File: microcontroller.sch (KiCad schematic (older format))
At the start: 18 parts, among them J6 I2C, J7 Conn_01x02, SW1 SW_Push, U3 ESP32-DEVKIT

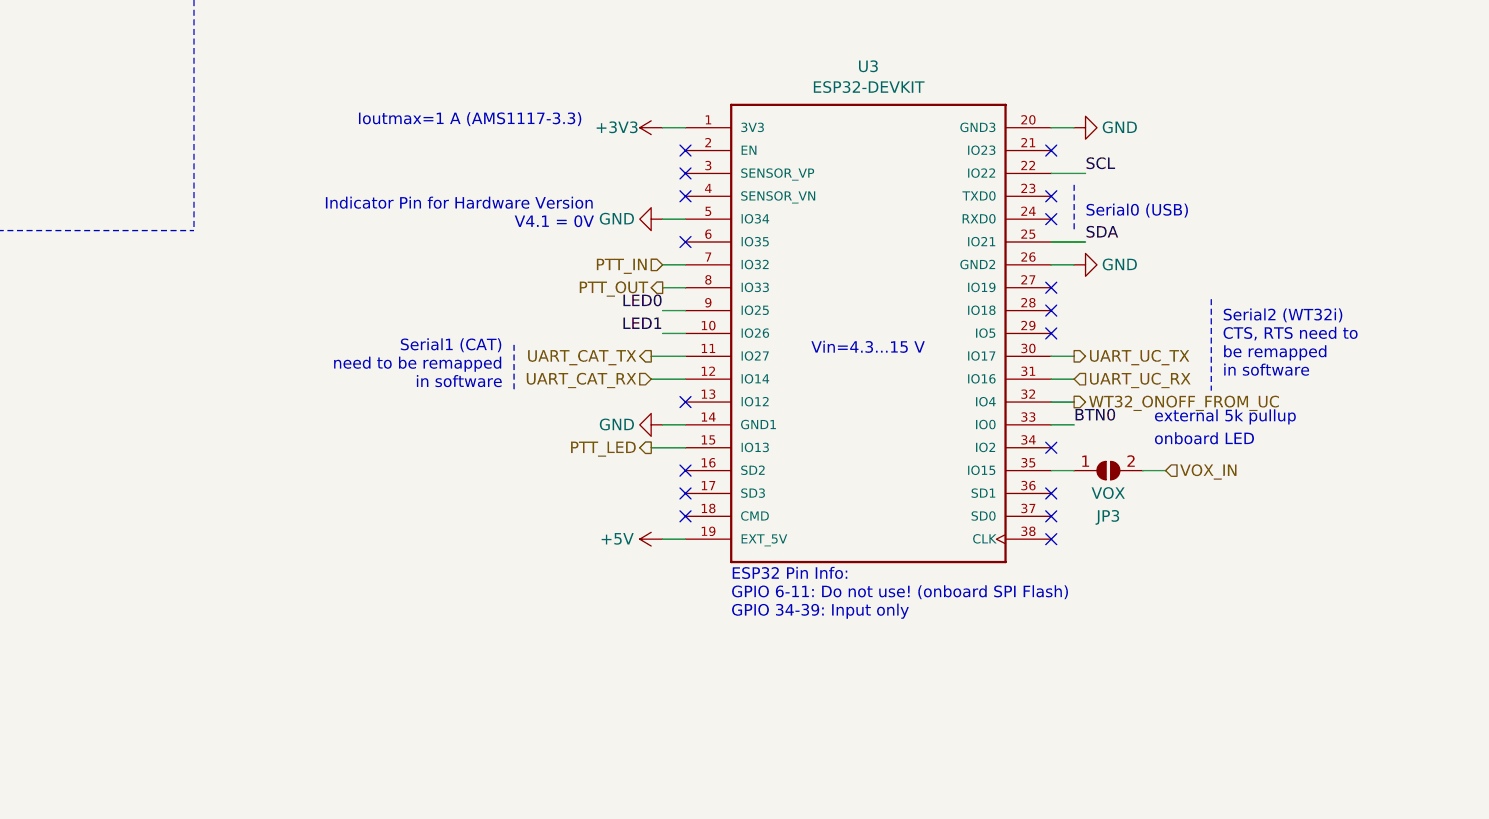
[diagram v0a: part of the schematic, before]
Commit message: Adding annotations for ADC1/2
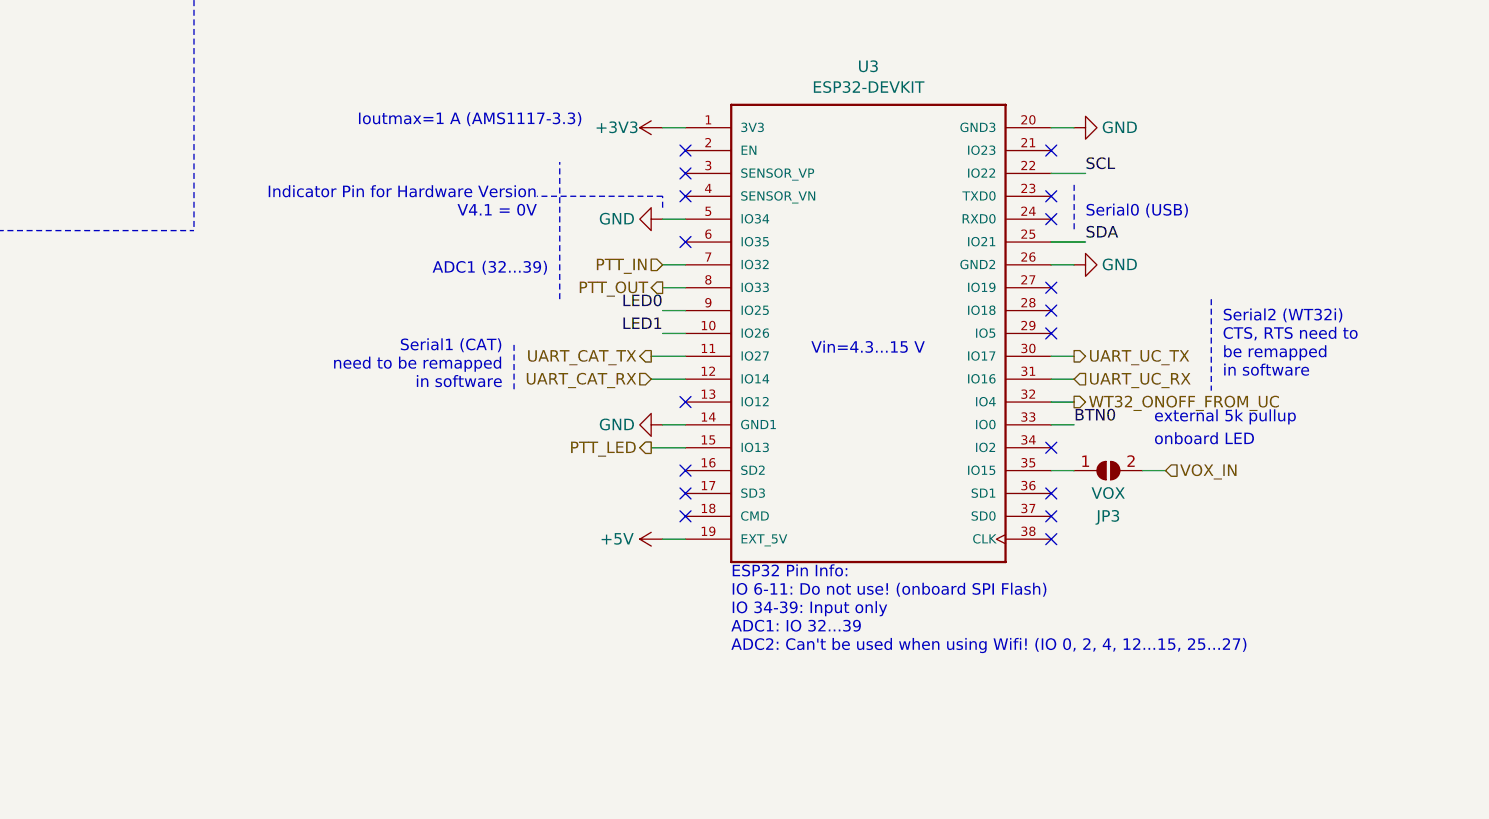
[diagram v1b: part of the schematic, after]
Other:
- note added: "ADC1 (32...39)"
- note added: "ESP32 Pin Info:\nIO 6-11: Do not use! (onboard SPI Flash)\nIO 34-39: Input only\nADC1: IO 32...39\nADC2: Can't be used when using Wifi! (IO 0, 2, 4, 12...15, 25...27)"
- note removed: "ESP32 Pin Info:\nGPIO 6-11: Do not use! (onboard SPI Flash)\nGPIO 34-39: Input only\n"
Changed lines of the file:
@@
 EESchema Schematic File Version 4
 LIBS:bt-trx-dev-board-cache
-EELAYER 30 0
+EELAYER 29 0
 EELAYER END
 $Descr A4 11693 8268
@@
 NoConn ~ 6900 1500
 NoConn ~ 6900 1600
-Text Notes 7100 3450 0    50   ~ 0
-ESP32 Pin Info:\nGPIO 6-11: Do not use! (onboard SPI Flash)\nGPIO 34-39: Input only\n
+Text Notes 7100 3600 0    50   ~ 0
+ESP32 Pin Info:\nIO 6-11: Do not use! (onboard SPI Flash)\nIO 34-39: Input only\nADC1: IO 32...39\nADC2: Can't be used when using Wifi! (IO 0, 2, 4, 12...15, 25...27)
 Wire Wire Line
 	8500 1300 8600 1300
@@
 	0    -1   -1   0
 $EndComp
-Text Notes 6500 1750 2    50   ~ 0
+Text Notes 6250 1700 2    50   ~ 0
 Indicator Pin for Hardware Version\nV4.1 = 0V
 Text HLabel 6750 2700 0    50   Output ~ 0
@@
 Wire Wire Line
 	8900 2800 9000 2800
+Wire Notes Line
+	6350 2050 6350 1450
+Text Notes 6300 1950 2    50   ~ 0
+ADC1 (32...39)
+Wire Notes Line style solid
+	6800 1650 6800 1600
+Wire Notes Line style solid
+	6800 1600 6250 1600
 $EndSCHEMATC

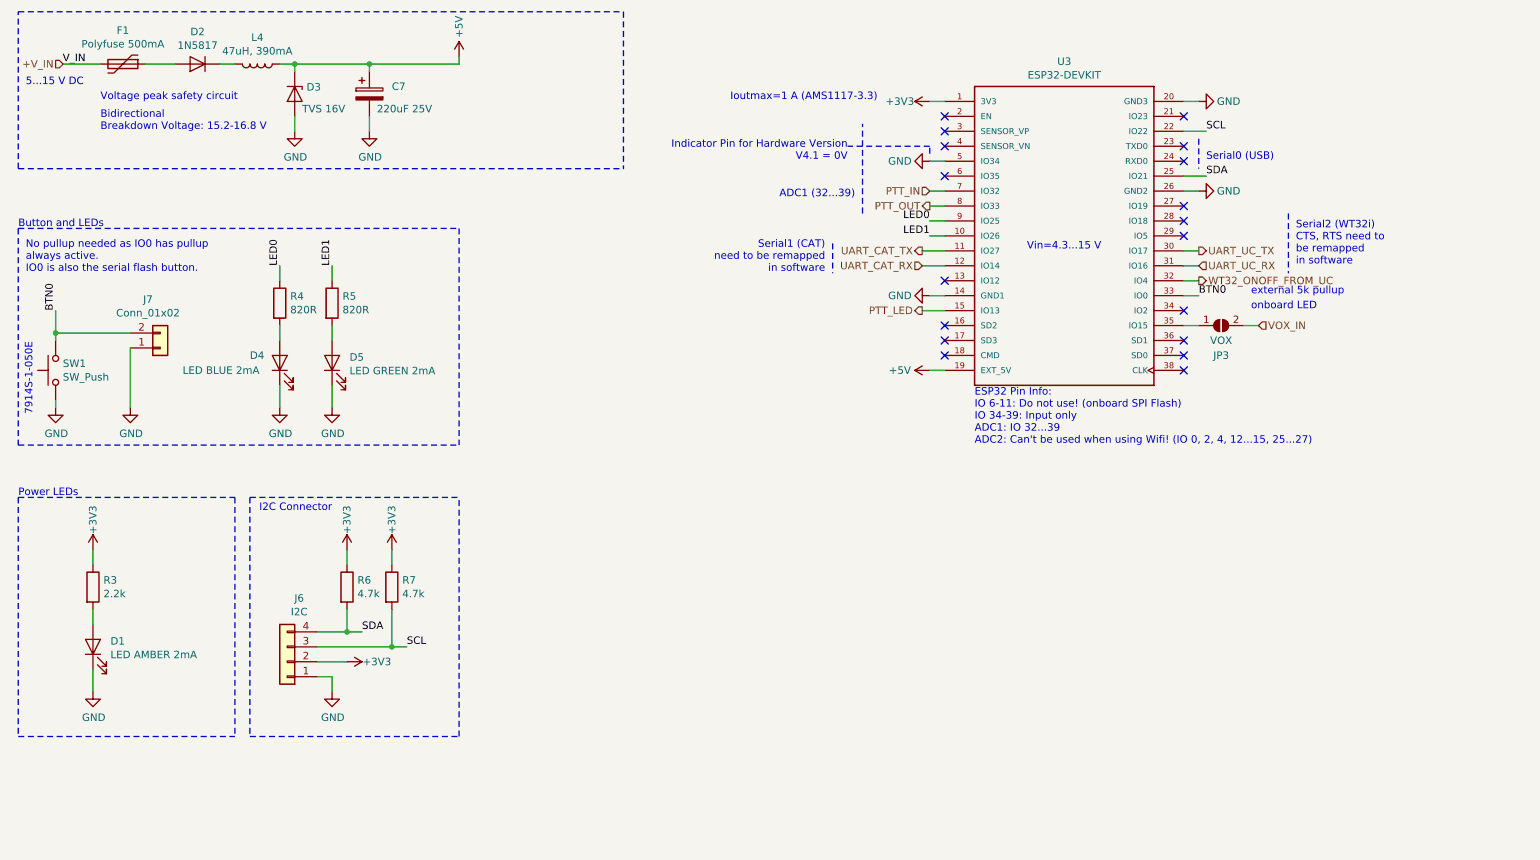
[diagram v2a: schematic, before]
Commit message: [#16] Move SW1 and VOX to usable Pins
* Moved SW1 form GPIO0 to GPIO18
* Added Pullup to SW1
* Moved VOX form GPIO2 to GPIO35
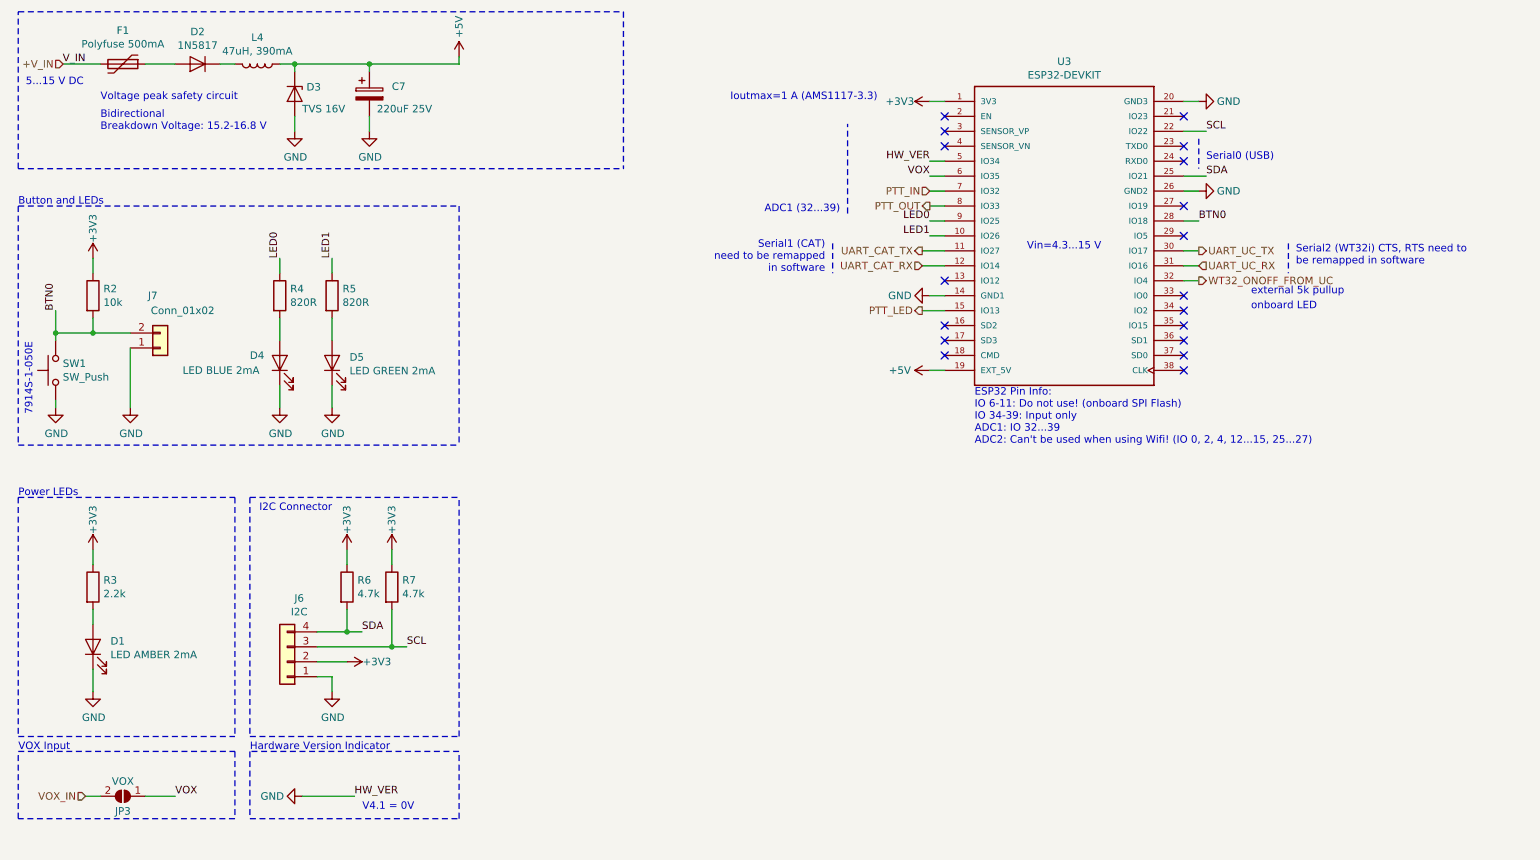
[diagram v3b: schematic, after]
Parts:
- added R2: 10k, Resistor_SMD:R_0805_2012Metric_Pad1.15x1.40mm_HandSolder, symbol Device:R
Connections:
- net +3V3: now also R2.1
- net BTN0: now also U3.28 (IO18), R2.2; no longer U3.33 (IO0)
- net at U3.35 (IO15): no longer JP3.1 (A)
- net VOX: now reaches U3.6 (IO35)
- net VOX: now also JP3.1 (A)
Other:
- note added: "Hardware Version Indicator"
- note added: "Serial2 (WT32i) CTS, RTS need to\nbe remapped in software"
- note added: "V4.1 = 0V"
- note added: "VOX Input"
- note removed: "Indicator Pin for Hardware Version\nV4.1 = 0V"
- note removed: "No pullup needed as IO0 has pullup\nalways active.\nIO0 is also the serial flash button."
- note removed: "Serial2 (WT32i)\nCTS, RTS need to\nbe remapped \nin software"
- moved on the sheet: JP3, R4, R5
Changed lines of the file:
@@
 L Device:R R?
 U 1 1 5C1540D9
-P 2450 2650
+P 2450 2600
 AR Path="/5C1540D9" Ref="R?"  Part="1"
 AR Path="/5C10B93A/5C1540D9" Ref="R4"  Part="1"
-F 0 "R4" H 2520 2696 50  0000 L CNN
-F 1 "820R" H 2520 2605 50  0000 L CNN
-F 2 "Resistor_SMD:R_0805_2012Metric_Pad1.15x1.40mm_HandSolder" V 2380 2650 50  0001 C CNN
-F 3 "~" H 2450 2650 50  0001 C CNN
-F 4 "603-RC0805JR-07820RL" H -2300 -2500 50  0001 C CNN "Mouser Best.Nr."
-	1    2450 2650
+F 0 "R4" H 2520 2646 50  0000 L CNN
+F 1 "820R" H 2520 2555 50  0000 L CNN
+F 2 "Resistor_SMD:R_0805_2012Metric_Pad1.15x1.40mm_HandSolder" V 2380 2600 50  0001 C CNN
+F 3 "~" H 2450 2600 50  0001 C CNN
+F 4 "603-RC0805JR-07820RL" H -2300 -2550 50  0001 C CNN "Mouser Best.Nr."
+	1    2450 2600
 	1    0    0    -1
 $EndComp
@@
 	2450 3200 2450 3350
 Wire Wire Line
-	2450 2500 2450 2400
-Text Label 2450 2400 1    50   ~ 0
+	2450 2450 2450 2350
+Text Label 2450 2350 1    50   ~ 0
 LED0
 $Comp
 L Device:R R?
 U 1 1 5C1540F1
-P 2800 2650
+P 2800 2600
 AR Path="/5C1540F1" Ref="R?"  Part="1"
 AR Path="/5C10B93A/5C1540F1" Ref="R5"  Part="1"
-F 0 "R5" H 2870 2696 50  0000 L CNN
-F 1 "820R" H 2870 2605 50  0000 L CNN
-F 2 "Resistor_SMD:R_0805_2012Metric_Pad1.15x1.40mm_HandSolder" V 2730 2650 50  0001 C CNN
-F 3 "~" H 2800 2650 50  0001 C CNN
-F 4 "603-RC0805JR-07820RL" H -2300 -2500 50  0001 C CNN "Mouser Best.Nr."
-	1    2800 2650
+F 0 "R5" H 2870 2646 50  0000 L CNN
+F 1 "820R" H 2870 2555 50  0000 L CNN
+F 2 "Resistor_SMD:R_0805_2012Metric_Pad1.15x1.40mm_HandSolder" V 2730 2600 50  0001 C CNN
+F 3 "~" H 2800 2600 50  0001 C CNN
+F 4 "603-RC0805JR-07820RL" H -2300 -2550 50  0001 C CNN "Mouser Best.Nr."
+	1    2800 2600
 	1    0    0    -1
 $EndComp
@@
 	2800 3200 2800 3350
 Wire Wire Line
-	2800 2800 2800 2900
-Wire Wire Line
-	2800 2500 2800 2400
-Text Label 2800 2400 1    50   ~ 0
+	2800 2450 2800 2350
+Text Label 2800 2350 1    50   ~ 0
 LED1
-Wire Notes Line
-	3650 2150 3650 3600
-Wire Notes Line
-	700  2150 700  3600
-Text Notes 700  2150 0    50   ~ 0
+Text Notes 700  2000 0    50   ~ 0
 Button and LEDs
 Text HLabel 1000 1050 0    50   Input ~ 0
@@
 Text HLabel 8600 2500 2    50   Output ~ 0
 WT32_ONOFF_FROM_UC
-Text Label 8600 2600 0    50   ~ 0
-BTN0
 Wire Wire Line
 	6800 2200 6900 2200
@@
 7914S-1-050E
 Wire Wire Line
-	2450 2800 2450 2900
-Wire Wire Line
 	1200 4700 1200 4800
 Text Notes 9250 2400 0    50   ~ 0
-Serial2 (WT32i)\nCTS, RTS need to\nbe remapped \nin software
+Serial2 (WT32i) CTS, RTS need to\nbe remapped in software
 Wire Notes Line
 	6150 2250 6150 2450
@@
 Text Notes 8950 2600 0    50   ~ 0
 external 5k pullup
-Wire Notes Line
-	9200 2050 9200 2450
 Wire Wire Line
 	8500 2300 8600 2300
@@
 NoConn ~ 8500 2000
 NoConn ~ 6900 2500
-NoConn ~ 8500 2100
+NoConn ~ 8500 2800
 Wire Wire Line
 	8500 2500 8600 2500
@@
 NoConn ~ 8500 2200
 Wire Wire Line
-	8500 2600 8600 2600
-Text Notes 750  2450 0    50   ~ 0
-No pullup needed as IO0 has pullup\nalways active.\nIO0 is also the serial flash button.
+	8500 2100 8600 2100
 $Comp
 L ESP32-DEVKITC-32D:ESP32-DEVKITC-32D U3
@@
 $EndComp
 Wire Notes Line
-	700  2150 3650 2150
+	700  2000 3650 2000
 Wire Notes Line
 	700  3600 3650 3600
@@
 U 1 1 5D923484
 P 1650 2950
-F 0 "J7" H 1568 2625 50  0000 C CNN
-F 1 "Conn_01x02" H 1568 2716 50  0000 C CNN
+F 0 "J7" H 1600 2600 50  0000 C CNN
+F 1 "Conn_01x02" H 1800 2700 50  0000 C CNN
 F 2 "Connector_PinHeader_2.54mm:PinHeader_1x02_P2.54mm_Vertical" H 1650 2950 50  0001 C CNN
 F 3 "~" H 1650 2950 50  0001 C CNN
@@
 	950  2700 950  2850
 Wire Wire Line
-	1450 2850 950  2850
+	1450 2850 1200 2850
 Connection ~ 950  2850
 Wire Wire Line
@@
 Wire Wire Line
 	1550 1050 1750 1050
-Wire Wire Line
-	6900 1700 6800 1700
 $Comp
 L power:GND #PWR?
 U 1 1 5D8F131B
-P 6800 1700
+P 2600 5950
 AR Path="/5D8F131B" Ref="#PWR?"  Part="1"
 AR Path="/5C10B93A/5D8F131B" Ref="#PWR0101"  Part="1"
-F 0 "#PWR0101" H 6800 1450 50  0001 C CNN
-F 1 "GND" V 6800 1500 50  0000 C CNN
-F 2 "" H 6800 1700 50  0001 C CNN
-F 3 "" H 6800 1700 50  0001 C CNN
-	1    6800 1700
+F 0 "#PWR0101" H 2600 5700 50  0001 C CNN
+F 1 "GND" V 2600 5750 50  0000 C CNN
+F 2 "" H 2600 5950 50  0001 C CNN
+F 3 "" H 2600 5950 50  0001 C CNN
+	1    2600 5950
 	0    1    1    0
 $EndComp
@@
 	0    -1   -1   0
 $EndComp
-Text Notes 6250 1700 2    50   ~ 0
-Indicator Pin for Hardware Version\nV4.1 = 0V
+Text Notes 3350 6050 2    50   ~ 0
+V4.1 = 0V
 Text HLabel 6750 2700 0    50   Output ~ 0
 PTT_LED
-NoConn ~ 6900 1800
 Wire Wire Line
 	6750 2700 6900 2700
-Text HLabel 9000 2800 2    50   Input ~ 0
+Text HLabel 1150 5950 0    50   Input ~ 0
 VOX_IN
 $Comp
 L Jumper:SolderJumper_2_Open JP3
 U 1 1 5D943D8B
-P 8750 2800
-F 0 "JP3" H 8750 2600 50  0000 C CNN
-F 1 "VOX" H 8750 2700 50  0000 C CNN
-F 2 "Jumper:SolderJumper-2_P1.3mm_Open_TrianglePad1.0x1.5mm" H 8750 2800 50  0001 C CNN
-F 3 "~" H 8750 2800 50  0001 C CNN
-	1    8750 2800
-	1    0    0    -1
+P 1400 5950
+F 0 "JP3" H 1400 6050 50  0000 C CNN
+F 1 "VOX" H 1400 5850 50  0000 C CNN
+F 2 "Jumper:SolderJumper-2_P1.3mm_Open_TrianglePad1.0x1.5mm" H 1400 5950 50  0001 C CNN
+F 3 "~" H 1400 5950 50  0001 C CNN
+	1    1400 5950
+	-1   0    0    1
 $EndComp
 NoConn ~ 8500 2700
 Wire Wire Line
-	8500 2800 8600 2800
-Wire Wire Line
-	8900 2800 9000 2800
-Wire Notes Line
-	6350 2050 6350 1450
-Text Notes 6300 1950 2    50   ~ 0
+	6900 1800 6800 1800
+Wire Wire Line
+	1250 5950 1150 5950
+Wire Notes Line
+	6250 2050 6250 1450
+Text Notes 6200 2050 2    50   ~ 0
 ADC1 (32...39)
-Wire Notes Line style solid
-	6800 1650 6800 1600
-Wire Notes Line style solid
-	6800 1600 6250 1600
+Wire Notes Line
+	9200 2250 9200 2450
+Text Label 8600 2100 0    50   ~ 0
+BTN0
+NoConn ~ 8500 2600
+Text Label 6800 1800 2    50   ~ 0
+VOX
+Wire Wire Line
+	2600 5950 2950 5950
+Wire Wire Line
+	1550 5950 1750 5950
+Text Label 1750 5950 0    50   ~ 0
+VOX
+Wire Notes Line
+	700  5650 2150 5650
+Wire Notes Line
+	2150 5650 2150 6100
+Wire Notes Line
+	2150 6100 700  6100
+Wire Notes Line
+	700  6100 700  5650
+Text Notes 700  5650 0    50   ~ 0
+VOX Input
+Wire Notes Line
+	2250 5650 2250 6100
+Wire Notes Line
+	2250 6100 3650 6100
+Wire Notes Line
+	3650 6100 3650 5650
+Wire Notes Line
+	3650 5650 2250 5650
+Text Notes 2250 5650 0    50   ~ 0
+Hardware Version Indicator
+Text Label 2950 5950 0    50   ~ 0
+HW_VER
+Wire Wire Line
+	6900 1700 6800 1700
+Text Label 6800 1700 2    50   ~ 0
+HW_VER
+$Comp
+L Device:R R?
+U 1 1 5D9F2FE4
+P 1200 2600
+AR Path="/5D9F2FE4" Ref="R?"  Part="1"
+AR Path="/5C10B93A/5D9F2FE4" Ref="R2"  Part="1"
+F 0 "R2" H 1270 2646 50  0000 L CNN
+F 1 "10k" H 1270 2555 50  0000 L CNN
+F 2 "Resistor_SMD:R_0805_2012Metric_Pad1.15x1.40mm_HandSolder" V 1130 2600 50  0001 C CNN
+F 3 "~" H 1200 2600 50  0001 C CNN
+F 4 "603-RC0805JR-07820RL" H -3550 -2550 50  0001 C CNN "Mouser Best.Nr."
+	1    1200 2600
+	1    0    0    -1
+$EndComp
+Connection ~ 1200 2850
+Wire Wire Line
+	1200 2850 950  2850
+$Comp
+L power:+3V3 #PWR?
+U 1 1 5D9F9842
+P 1200 2350
+AR Path="/5D9F9842" Ref="#PWR?"  Part="1"
+AR Path="/5C10B93A/5D9F9842" Ref="#PWR040"  Part="1"
+F 0 "#PWR040" H 1200 2200 50  0001 C CNN
+F 1 "+3V3" V 1200 2550 50  0000 C CNN
+F 2 "" H 1200 2350 50  0001 C CNN
+F 3 "" H 1200 2350 50  0001 C CNN
+	1    1200 2350
+	1    0    0    -1
+$EndComp
+Wire Wire Line
+	2450 2750 2450 2900
+Wire Wire Line
+	2800 2750 2800 2900
+Wire Wire Line
+	1200 2750 1200 2850
+Wire Wire Line
+	1200 2350 1200 2450
+Wire Notes Line
+	3650 2000 3650 3600
+Wire Notes Line
+	700  2000 700  3600
 $EndSCHEMATC

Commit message: [#18] Changed SW1 from SMD to TH
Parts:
- J7: Mouser Best.Nr. (none) -> 855-M20-9990246
- R2: Mouser Best.Nr. 603-RC0805JR-07820RL -> 603-RC0805FR-0710KL
- SW1: footprint Button_Switch_SMD:Panasonic_EVQPUL_EVQPUC -> Button_Switch_THT:SW_Tactile_SKHH_Angled; Mouser Best.Nr. 667-EVQ-PUL02K -> 611-PTS645VK832
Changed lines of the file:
@@
 F 0 "SW1" V 996 3052 50  0000 R CNN
 F 1 "SW_Push" V 905 3052 50  0000 R CNN
-F 2 "Button_Switch_SMD:Panasonic_EVQPUL_EVQPUC" H 950 3300 50  0001 C CNN
+F 2 "Button_Switch_THT:SW_Tactile_SKHH_Angled" H 950 3300 50  0001 C CNN
 F 3 "" H 950 3300 50  0001 C CNN
-F 4 " 667-EVQ-PUL02K" H -2700 -2500 50  0001 C CNN "Mouser Best.Nr."
+F 4 " 611-PTS645VK832" H -2700 -2500 50  0001 C CNN "Mouser Best.Nr."
 	1    950  3100
 	0    -1   -1   0
@@
 F 2 "Connector_PinHeader_2.54mm:PinHeader_1x02_P2.54mm_Vertical" H 1650 2950 50  0001 C CNN
 F 3 "~" H 1650 2950 50  0001 C CNN
+F 4 " 855-M20-9990246" H 1650 2950 50  0001 C CNN "Mouser Best.Nr."
 	1    1650 2950
 	1    0    0    1
@@
 F 2 "Resistor_SMD:R_0805_2012Metric_Pad1.15x1.40mm_HandSolder" V 1130 2600 50  0001 C CNN
 F 3 "~" H 1200 2600 50  0001 C CNN
-F 4 "603-RC0805JR-07820RL" H -3550 -2550 50  0001 C CNN "Mouser Best.Nr."
+F 4 " 603-RC0805FR-0710KL" H -3550 -2550 50  0001 C CNN "Mouser Best.Nr."
 	1    1200 2600
 	1    0    0    -1

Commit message: Replaced ESP32 DevKitC in BOM
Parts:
- U3: Mouser Best.Nr. 485-3591 -> 356-ESP32-DEVKITC32D
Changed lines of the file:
@@
 F 2 "nodemcu_esp-32s:ESP32-DEVKITC-32D" H 7700 2200 50  0001 L BNN
 F 3 "None" H 7700 2200 50  0001 L BNN
-F 4 " 485-3591 " H 7700 2200 50  0001 C CNN "Mouser Best.Nr."
+F 4 " 356-ESP32-DEVKITC32D " H 7700 2200 50  0001 C CNN "Mouser Best.Nr."
 	1    7700 2200
 	1    0    0    -1
